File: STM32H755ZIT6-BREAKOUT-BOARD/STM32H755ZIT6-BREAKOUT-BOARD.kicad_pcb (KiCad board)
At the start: 2 copper layers, 1 part, among them U1 STM32H755ZITx

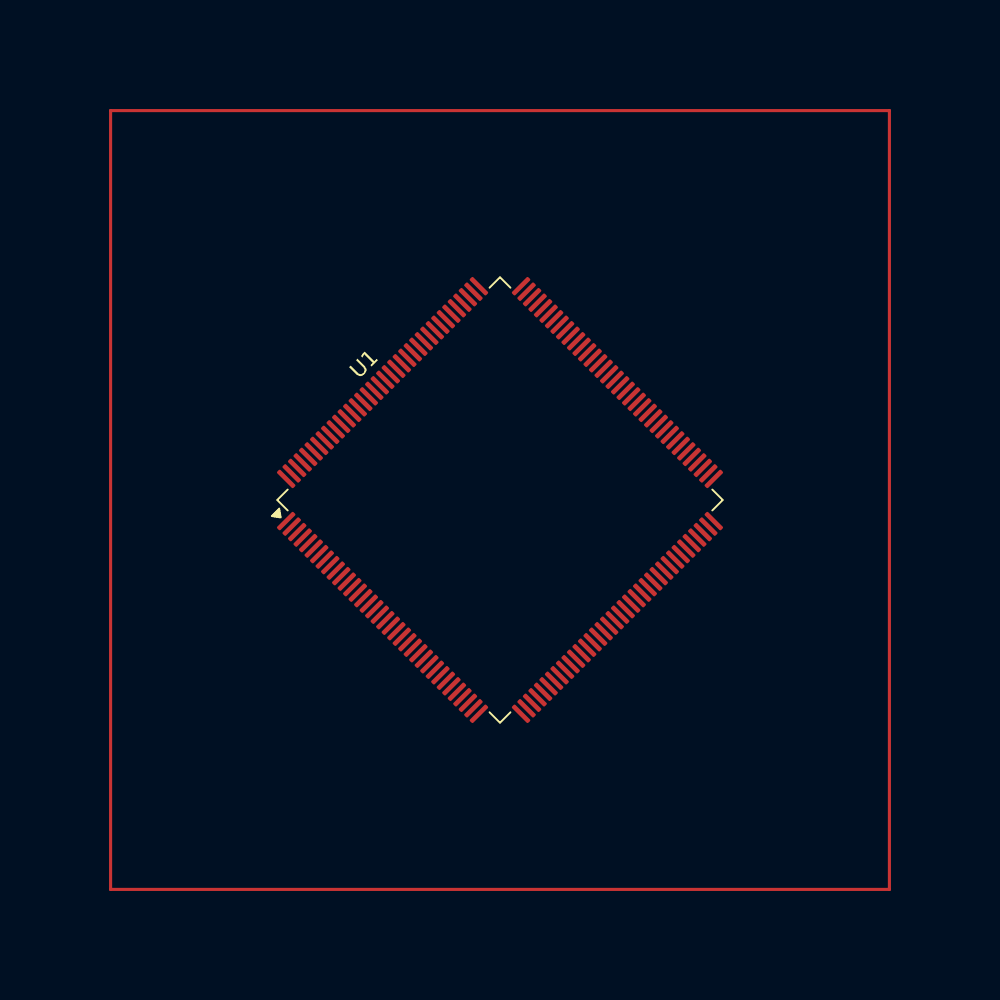
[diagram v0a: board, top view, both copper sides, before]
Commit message: pinheaders
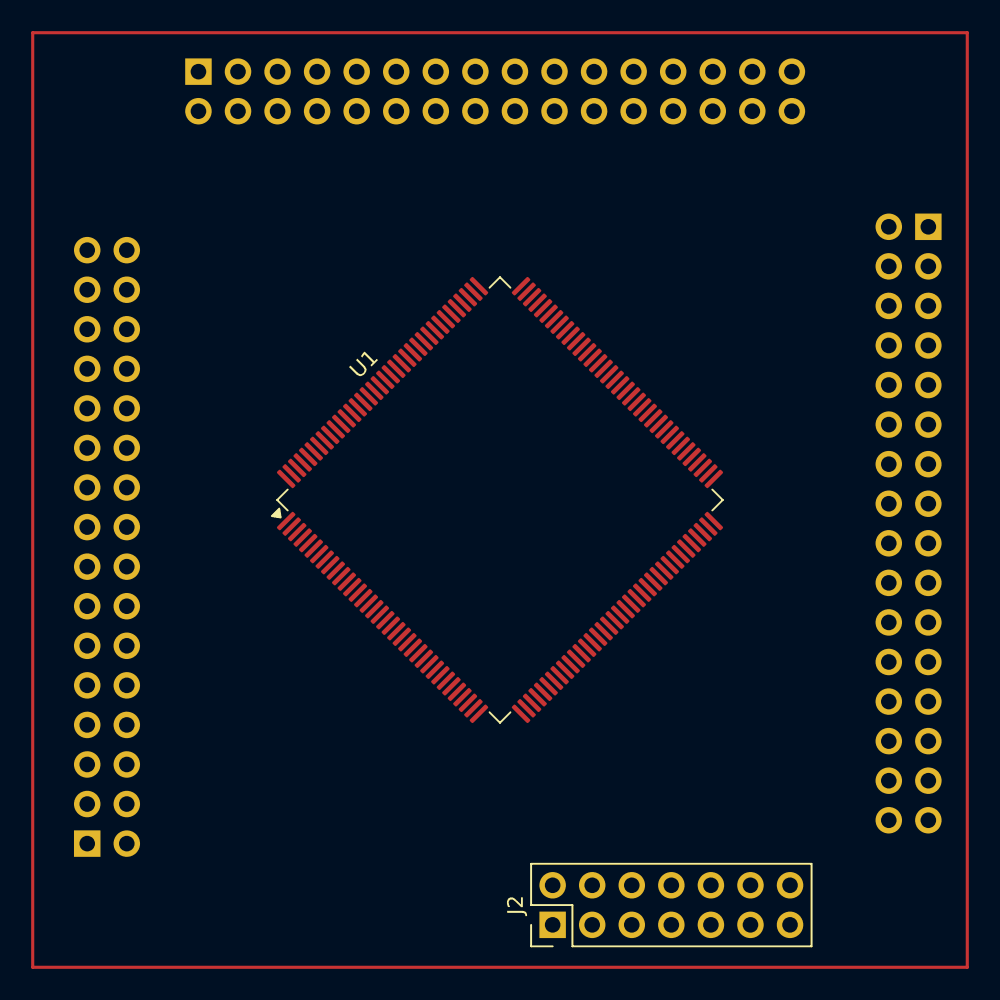
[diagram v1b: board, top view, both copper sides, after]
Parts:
- added J1: Conn_02x16_Odd_Even, Connector_PinHeader_2.54mm:PinHeader_2x16_P2.54mm_Vertical, B.Cu at (127.5, 82.5)
- added J2: Conn_ST_STDC14, Connector_PinHeader_2.54mm:PinHeader_2x07_P2.54mm_Vertical, F.Cu at (103.4, 127.3)
- added J3: Conn_02x16_Odd_Even, Connector_PinHeader_2.54mm:PinHeader_2x16_P2.54mm_Vertical, B.Cu at (80.6, 72.5)
- added J4: Conn_02x16_Odd_Even, Connector_PinHeader_2.54mm:PinHeader_2x16_P2.54mm_Vertical, B.Cu at (73.5, 122.1)
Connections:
- U1 pad 1: unconnected-(U1-PE2-Pad1) -> /PE2
- U1 pad 10: unconnected-(U1-PC14-Pad10) -> /PC14
- U1 pad 100: unconnected-(U1-PA11-Pad100) -> /PA11
- U1 pad 101: unconnected-(U1-PA12-Pad101) -> /PA12
- U1 pad 102: unconnected-(U1-PA13-Pad102) -> /JTMS/SWDIO
- U1 pad 107: unconnected-(U1-PA14-Pad107) -> /JTDO/SWO
- U1 pad 108: unconnected-(U1-PA15-Pad108) -> /JTDI
- U1 pad 109: unconnected-(U1-PC10-Pad109) -> /PC10
- U1 pad 11: unconnected-(U1-PC15-Pad11) -> /PC15
- U1 pad 110: unconnected-(U1-PC11-Pad110) -> /PC11
- U1 pad 111: unconnected-(U1-PC12-Pad111) -> /PC12
- U1 pad 112: unconnected-(U1-PD0-Pad112) -> /PD0
- U1 pad 113: unconnected-(U1-PD1-Pad113) -> /PD1
- U1 pad 114: unconnected-(U1-PD2-Pad114) -> /PD2
- U1 pad 115: unconnected-(U1-PD3-Pad115) -> /PD3
- U1 pad 116: unconnected-(U1-PD4-Pad116) -> /PD4
- U1 pad 117: unconnected-(U1-PD5-Pad117) -> /PD5
- U1 pad 120: unconnected-(U1-PD6-Pad120) -> /PD6
- U1 pad 121: unconnected-(U1-PD7-Pad121) -> /PD7
- U1 pad 122: unconnected-(U1-PG9-Pad122) -> /PG9
- U1 pad 123: unconnected-(U1-PG10-Pad123) -> /PG10
- U1 pad 124: unconnected-(U1-PG11-Pad124) -> /PG11
- U1 pad 125: unconnected-(U1-PG12-Pad125) -> /PG12
- U1 pad 126: unconnected-(U1-PG13-Pad126) -> /PG13
- U1 pad 127: unconnected-(U1-PG14-Pad127) -> /PG14
- U1 pad 130: unconnected-(U1-PB3-Pad130) -> /JTDO/SWO
- U1 pad 131: unconnected-(U1-PB4-Pad131) -> /PB4
- U1 pad 132: unconnected-(U1-PB5-Pad132) -> /PB5
- U1 pad 133: unconnected-(U1-PB6-Pad133) -> /PB6
- U1 pad 134: unconnected-(U1-PB7-Pad134) -> /PB7
- U1 pad 135: unconnected-(U1-BOOT0-Pad135) -> /BOOT0
- U1 pad 136: unconnected-(U1-PB8-Pad136) -> /PB8
- U1 pad 137: unconnected-(U1-PB9-Pad137) -> /PB9
- U1 pad 138: unconnected-(U1-PE0-Pad138) -> /PE0
- U1 pad 139: unconnected-(U1-PE1-Pad139) -> /PE1
- U1 pad 142: unconnected-(U1-PDR_ON-Pad142) -> /PDR_ON
- U1 pad 2: unconnected-(U1-PE3-Pad2) -> /PE3
- U1 pad 20: unconnected-(U1-PF6-Pad20) -> /PF6
- U1 pad 21: unconnected-(U1-PF7-Pad21) -> /PF7
- U1 pad 22: unconnected-(U1-PF8-Pad22) -> /PF8
- U1 pad 23: unconnected-(U1-PF9-Pad23) -> /PF9
- U1 pad 24: unconnected-(U1-PF10-Pad24) -> /PF10
- U1 pad 28: unconnected-(U1-PC0-Pad28) -> /PC0
- U1 pad 29: unconnected-(U1-PC1-Pad29) -> /PC1
- U1 pad 3: unconnected-(U1-PE4-Pad3) -> /PE4
- U1 pad 30: unconnected-(U1-PC2_C-Pad30) -> /PC2
- U1 pad 31: unconnected-(U1-PC3_C-Pad31) -> /PC3
- U1 pad 37: unconnected-(U1-PA0-Pad37) -> /PA0
- U1 pad 38: unconnected-(U1-PA1-Pad38) -> /PA1
- U1 pad 39: unconnected-(U1-PA2-Pad39) -> /PA2
- U1 pad 4: unconnected-(U1-PE5-Pad4) -> /PE5
- U1 pad 40: unconnected-(U1-PA3-Pad40) -> /PA3
- U1 pad 43: unconnected-(U1-PA4-Pad43) -> /PA4
- U1 pad 44: unconnected-(U1-PA5-Pad44) -> /PA5
- U1 pad 45: unconnected-(U1-PA6-Pad45) -> /PA6
- U1 pad 46: unconnected-(U1-PA7-Pad46) -> /PA7
- U1 pad 47: unconnected-(U1-PC4-Pad47) -> /PC4
- U1 pad 48: unconnected-(U1-PC5-Pad48) -> /PC5
- U1 pad 49: unconnected-(U1-PB0-Pad49) -> /PB0
- U1 pad 5: unconnected-(U1-PE6-Pad5) -> /PE6
- U1 pad 50: unconnected-(U1-PB1-Pad50) -> /PB1
- U1 pad 51: unconnected-(U1-PB2-Pad51) -> /PB2
- U1 pad 52: unconnected-(U1-PF11-Pad52) -> /PF11
- U1 pad 53: unconnected-(U1-PF14-Pad53) -> /PF14
- U1 pad 54: unconnected-(U1-PF15-Pad54) -> /PF15
- U1 pad 57: unconnected-(U1-PE7-Pad57) -> /PE7
- U1 pad 58: unconnected-(U1-PE8-Pad58) -> /PE8
- U1 pad 59: unconnected-(U1-PE9-Pad59) -> /PE9
- U1 pad 60: unconnected-(U1-PE10-Pad60) -> /PE10
- U1 pad 61: unconnected-(U1-PE11-Pad61) -> /PE11
- U1 pad 62: unconnected-(U1-PE12-Pad62) -> /PE12
- U1 pad 63: unconnected-(U1-PE13-Pad63) -> /PE13
- U1 pad 64: unconnected-(U1-PE14-Pad64) -> /PE14
- U1 pad 65: unconnected-(U1-PE15-Pad65) -> /PE15
- U1 pad 66: unconnected-(U1-PB10-Pad66) -> /PB10
- U1 pad 67: unconnected-(U1-PB11-Pad67) -> /PB11
- U1 pad 72: unconnected-(U1-PB12-Pad72) -> /PB12
- U1 pad 73: unconnected-(U1-PB13-Pad73) -> /PB13
- U1 pad 76: unconnected-(U1-PD8-Pad76) -> /PD8
- U1 pad 77: unconnected-(U1-PD9-Pad77) -> /PD9
- U1 pad 78: unconnected-(U1-PD10-Pad78) -> /PD10
- U1 pad 81: unconnected-(U1-PD11-Pad81) -> /PD11
- U1 pad 82: unconnected-(U1-PD12-Pad82) -> /PD12
- U1 pad 83: unconnected-(U1-PD13-Pad83) -> /PD13
- U1 pad 84: unconnected-(U1-PD14-Pad84) -> /PD14
- U1 pad 85: unconnected-(U1-PD15-Pad85) -> /PD15
- U1 pad 86: unconnected-(U1-PG6-Pad86) -> /PG6
- U1 pad 87: unconnected-(U1-PG7-Pad87) -> /PG7
- U1 pad 88: unconnected-(U1-PG8-Pad88) -> /PG8
- U1 pad 9: unconnected-(U1-PC13-Pad9) -> /PC13
- U1 pad 93: unconnected-(U1-PC6-Pad93) -> /PC6
- U1 pad 94: unconnected-(U1-PC7-Pad94) -> /PC7
- U1 pad 95: unconnected-(U1-PC8-Pad95) -> /PC8
- U1 pad 96: unconnected-(U1-PC9-Pad96) -> /PC9
- U1 pad 97: unconnected-(U1-PA8-Pad97) -> /PA8
- U1 pad 98: unconnected-(U1-PA9-Pad98) -> /PA9
- U1 pad 99: unconnected-(U1-PA10-Pad99) -> /PA10
